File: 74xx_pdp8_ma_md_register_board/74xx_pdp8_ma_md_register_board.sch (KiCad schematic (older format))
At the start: 39 parts, among them P1 DIL24, P2 DIL24, P3 DIL24, P4 DIL24, P5 DIL24, U1 74HC125, U10 74HC04, U11 74HC163, U12 74HC163, U13 74HC163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

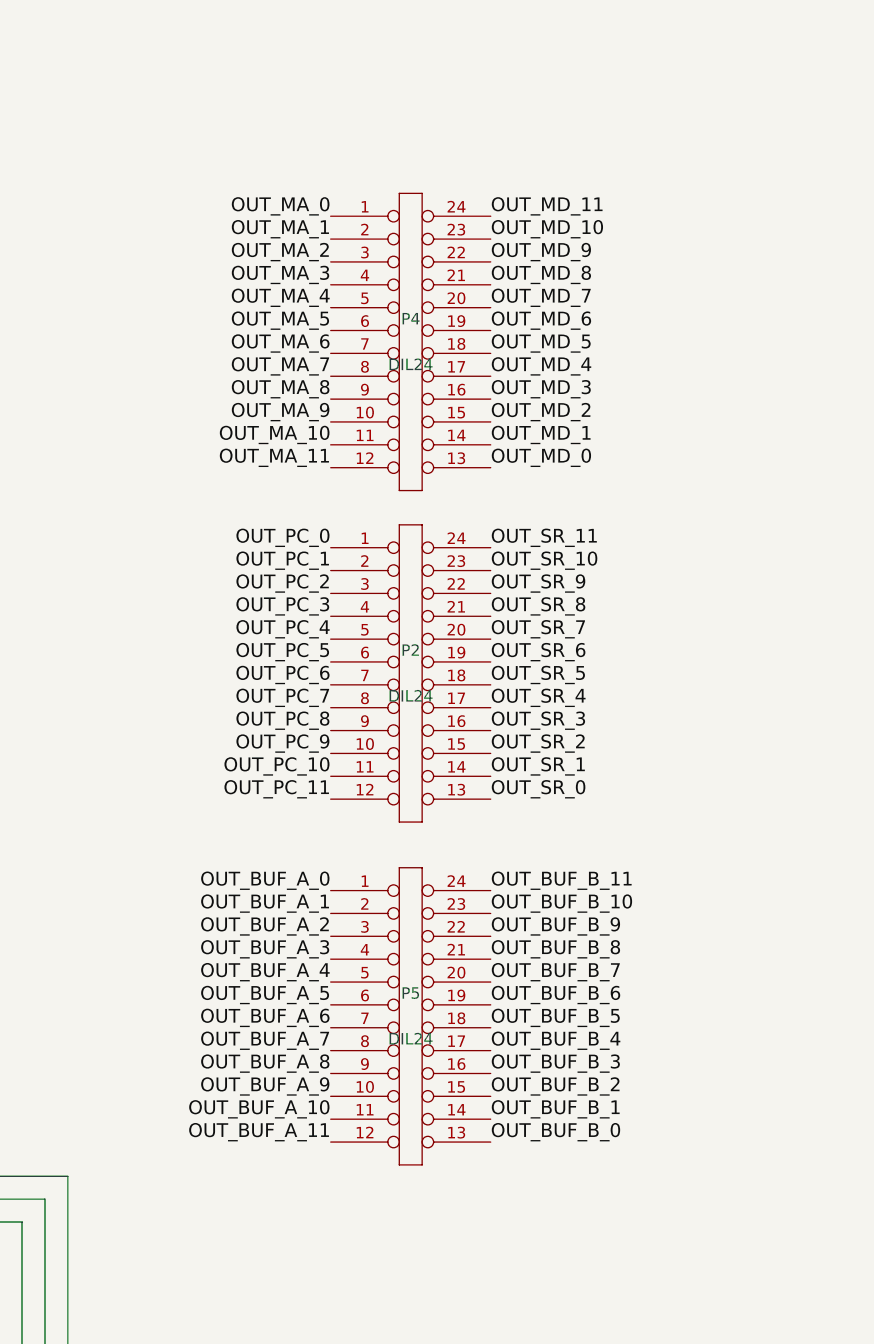
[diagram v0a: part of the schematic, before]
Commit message: Big changes - elected to switch to board interconnections along one long edge only. Boards to connect to backplane via right-angled DIL connectors. Both register boards and register mux boards thusly modified.
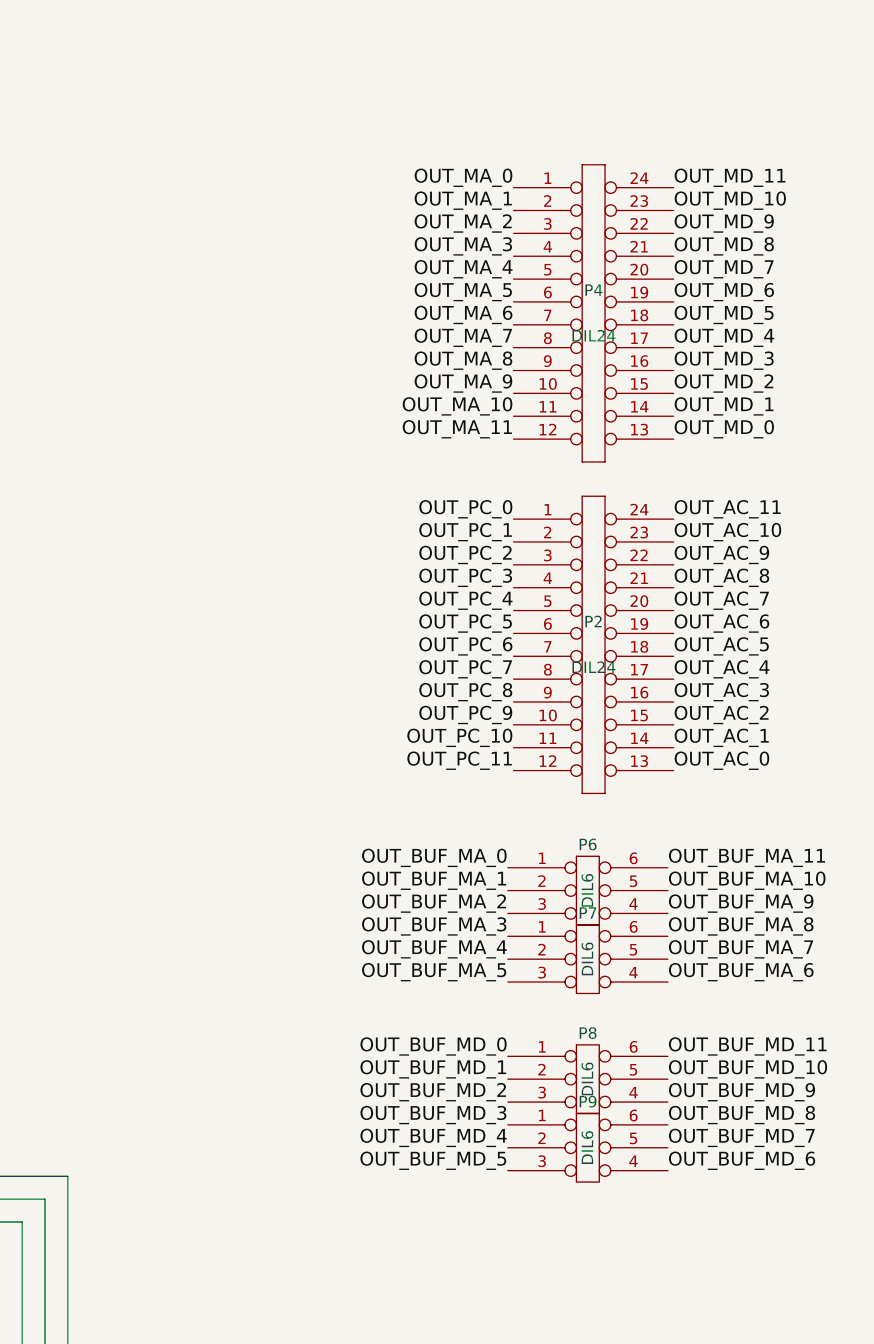
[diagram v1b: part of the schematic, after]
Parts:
- removed P5: DIL24, Socket_Strips:Socket_Strip_Straight_2x12, symbol DIL24
- added P6, P7, P8, P9: DIL6, Socket_Strips:Socket_Strip_Straight_2x03, symbol DIL6
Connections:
- net OUT_BUF_MA_0: now also P6.1 (P1)
- net OUT_BUF_MA_1: now also P6.2 (P2)
- net OUT_BUF_MA_10: now also P6.5 (P5)
- net OUT_BUF_MA_11: now also P6.6 (P6)
- net OUT_BUF_MA_2: now also P6.3 (P3)
- net OUT_BUF_MA_3: now also P7.1 (P1)
- net OUT_BUF_MA_4: now also P7.2 (P2)
- net OUT_BUF_MA_5: now also P7.3 (P3)
- net OUT_BUF_MA_6: now also P7.4 (P4)
- net OUT_BUF_MA_7: now also P7.5 (P5)
- net OUT_BUF_MA_8: now also P7.6 (P6)
- net OUT_BUF_MA_9: now also P6.4 (P4)
- net OUT_BUF_MD_0: now also P8.1 (P1)
- net OUT_BUF_MD_1: now also P8.2 (P2)
- net OUT_BUF_MD_10: now also P8.5 (P5)
- net OUT_BUF_MD_11: now also P8.6 (P6)
- net OUT_BUF_MD_2: now also P8.3 (P3)
- net OUT_BUF_MD_3: now also P9.1 (P1)
- net OUT_BUF_MD_4: now also P9.2 (P2)
- net OUT_BUF_MD_5: now also P9.3 (P3)
- net OUT_BUF_MD_6: now also P9.4 (P4)
- net OUT_BUF_MD_7: now also P9.5 (P5)
- net OUT_BUF_MD_8: now also P9.6 (P6)
- net OUT_BUF_MD_9: now also P8.4 (P4)
- net OUT_SR_0 renamed OUT_AC_0
- net OUT_SR_1 renamed OUT_AC_1
- net OUT_SR_10 renamed OUT_AC_10
- net OUT_SR_11 renamed OUT_AC_11
- net OUT_SR_2 renamed OUT_AC_2
- net OUT_SR_3 renamed OUT_AC_3
- net OUT_SR_4 renamed OUT_AC_4
- net OUT_SR_5 renamed OUT_AC_5
- net OUT_SR_6 renamed OUT_AC_6
- net OUT_SR_7 renamed OUT_AC_7
- net OUT_SR_8 renamed OUT_AC_8
- net OUT_SR_9 renamed OUT_AC_9
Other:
- moved on the sheet: P2, P4
